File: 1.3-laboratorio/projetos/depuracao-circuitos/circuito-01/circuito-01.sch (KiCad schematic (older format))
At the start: 22 parts, among them J1 Conn_01x07_Male, J2 Conn_01x07_Male, J3 Conn_01x07_Male, J4 Conn_01x07_Male, J5 Conn_01x07_Male, J6 Conn_01x07_Male, J7 Conn_01x05, J8 Conn_01x05, P1 CONN_01X02, SW1 SW_DIP_x04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

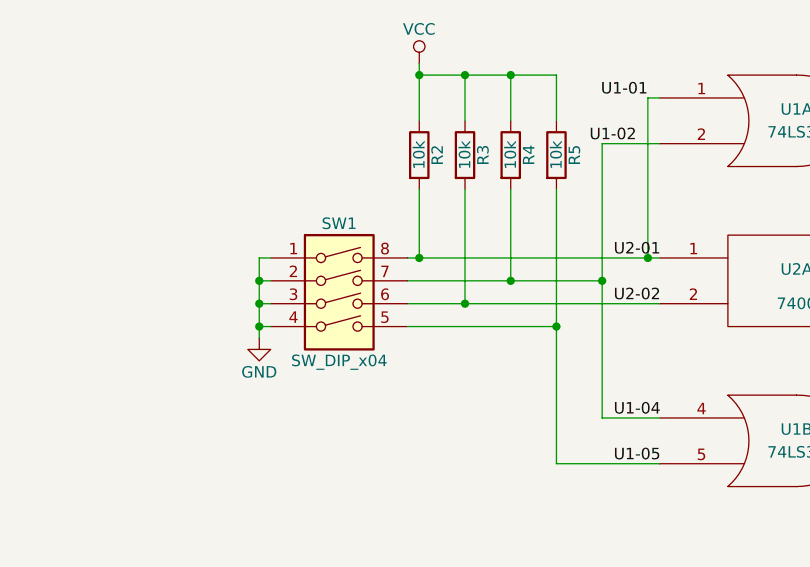
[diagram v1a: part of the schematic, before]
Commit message: Revisão final das versões do esquema elétrico do Circuito para Depuração 01. Correções de identificação de variáveis de entrada realizadas, incluindo as correções nas expressões e Tabela-Verdade.
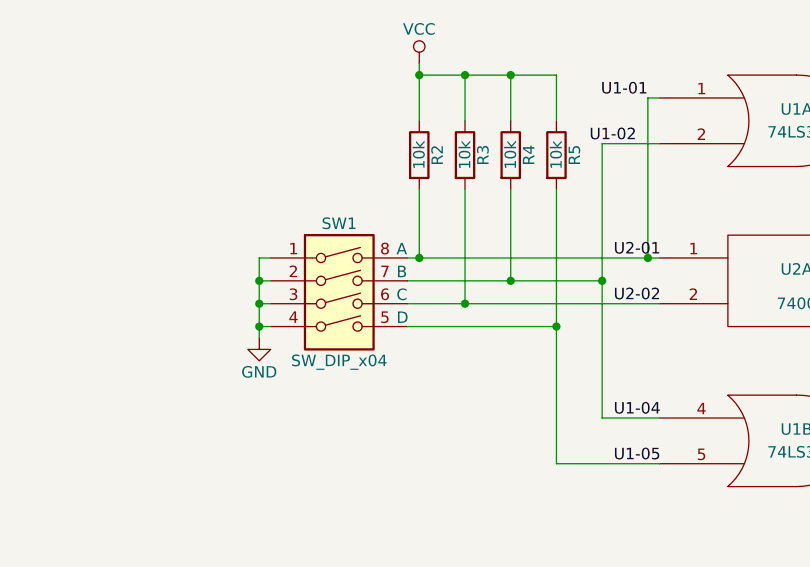
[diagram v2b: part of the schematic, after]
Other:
- note added: "A"
- note added: "B"
- note added: "C"
- note added: "D"
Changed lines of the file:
@@
 Sheet 1 1
 Title "Depuração de Circuitos - Circuito 01"
-Date "2019-04-21"
-Rev "02"
-Comp "ETE102 - Fundamentos de Circuitos Digitais"
+Date "2021-01-30"
+Rev "02.1"
+Comp "ETE102 - Fundamentos de Circuitos Digitais / IMT"
 Comment1 "Licença: CC-BY-SA (http://creativecommons.org/licenses/by-sa/4.0/)"
 Comment2 ""
 Comment3 ""
-Comment4 "(Circuito sem Defeito)"
+Comment4 "(Circuito sem defeito. Referência para a PCI sem defeito.)"
 $EndDescr
 $Comp
@@
 	-1   0    0    -1
 $EndComp
+Text Notes 2850 3600 0    50   ~ 0
+A
+Text Notes 2850 3700 0    50   ~ 0
+B
+Text Notes 2850 3800 0    50   ~ 0
+C
+Text Notes 2850 3900 0    50   ~ 0
+D
 $EndSCHEMATC
